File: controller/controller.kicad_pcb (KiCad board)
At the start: 2 copper layers, 105 x 42 mm, 46 parts, among them J1 j0011d21bnl, J2 swim_header, SW1 SW_left, SW2 SW_a0, SW3 SW_right, SW4 SW_a1, SW5 SW_up, SW6 SW_back_r, SW7 SW_down, SW8 SW_back_l, U1 74HCT541, U2 STM8L101F3P

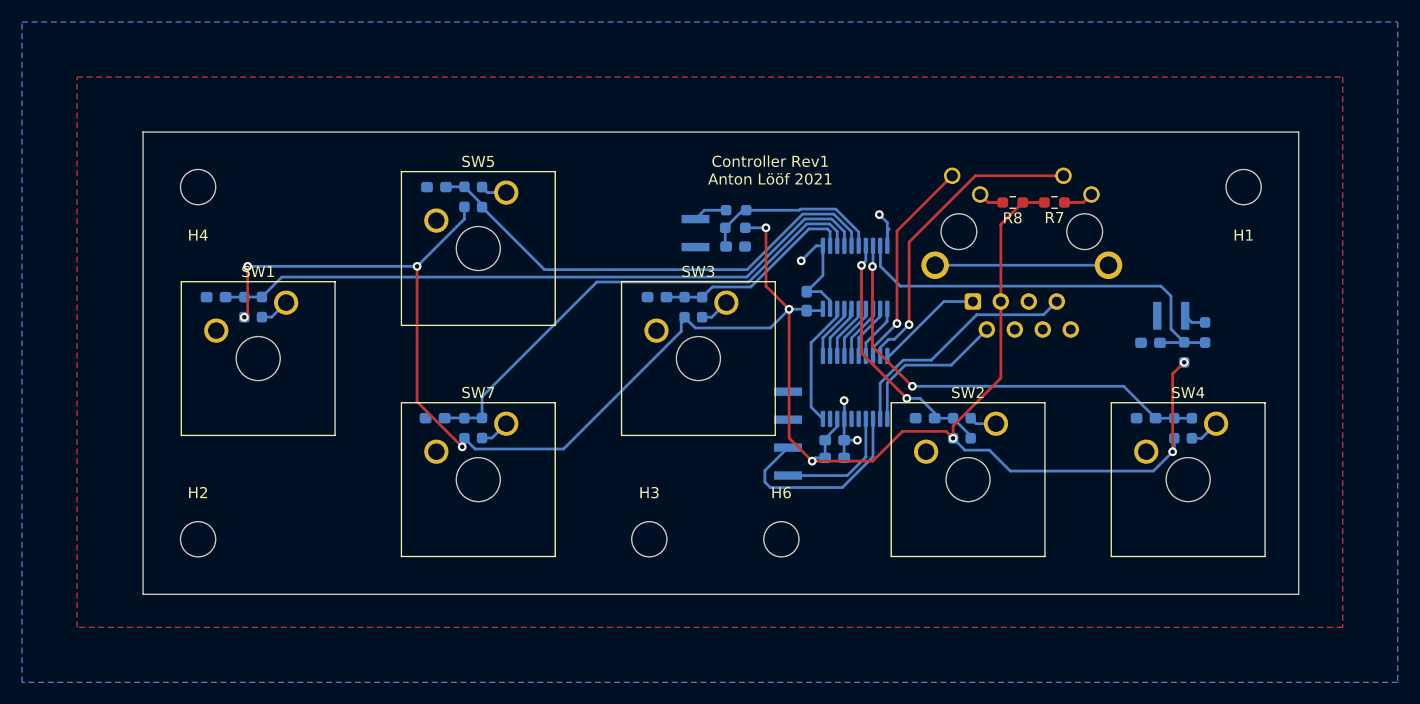
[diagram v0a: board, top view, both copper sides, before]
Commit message: Rev 2 controller PCB
Now uses correct rj45 footprint.
Leds should work!
Added 1 more mounting hole (H5)
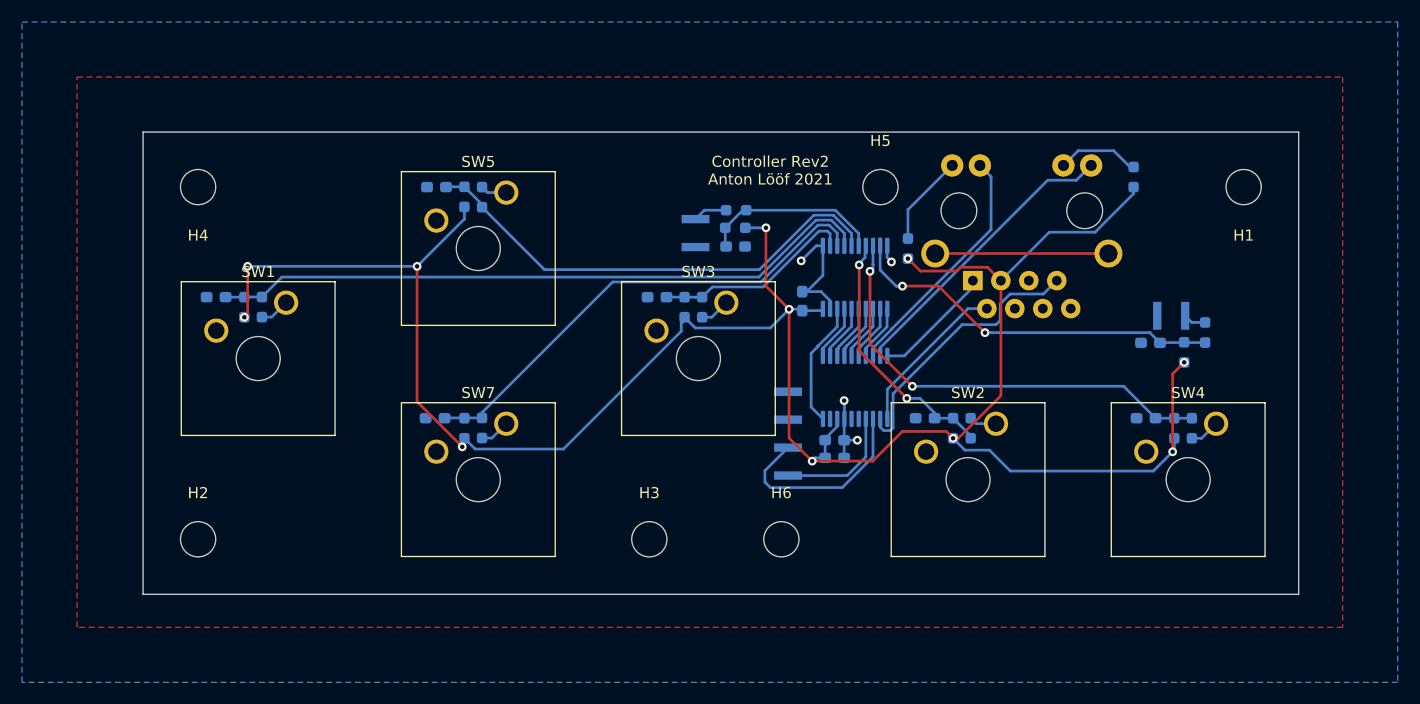
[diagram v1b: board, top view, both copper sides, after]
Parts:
- added H5: MountingHole, MountingHole:MountingHole_3.2mm_M3, F.Cu at (120.0, 57.5)
- J1: footprint Connector_RJ:RJ45_Cetus_J1B1211CCD_Horizontal -> Connector_RJ:RJ45_BEL_SS74301-00x_Vertical
- R7, R8: moved to B.Cu
- moved R7 14.0 mm to (122.5, 63.1), turned to 90 degrees
- moved R8 11.2 mm to (143.0, 56.6), turned to 90 degrees
- moved J1 1.90 mm to (128.4, 66.0)
- moved C9 0.40 mm to (112.9, 67.9)
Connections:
- U2 pad 18: rxled -> txled
- U2 pad 19: txled -> rxled
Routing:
- net 3v3: track 188.8 -> 204.7 mm, vias 10 -> 11
- net rxled: track 19.3 -> 26.8 mm, vias 1 -> 0
- net txled: track 28.3 -> 22.2 mm, vias 1 -> 0
- net Net-(J1-Pad12): track 2.75 -> 8.31 mm
- net Net-(J1-Pad10): track 2.34 -> 7.54 mm
- net sw_back_r: track 38.2 -> 35.1 mm, vias 0 -> 2
- net connected: track 22.4 -> 25.3 mm
- net GND: track 21.7 -> 19.1 mm
- net tx: track 9.82 -> 11.0 mm
- net sw_down: track 45.7 -> 44.7 mm
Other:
- board text added: "Controller Rev2 Anton Lööf 2021"
- board text removed: "Controller Rev1 Anton Lööf 2021"
